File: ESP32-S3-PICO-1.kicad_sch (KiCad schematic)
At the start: 13 parts, among them CN3 Conn_Coaxial_Small, U5 ESP32-S3-PICO-1-N8R8, U6 BGS12WN6

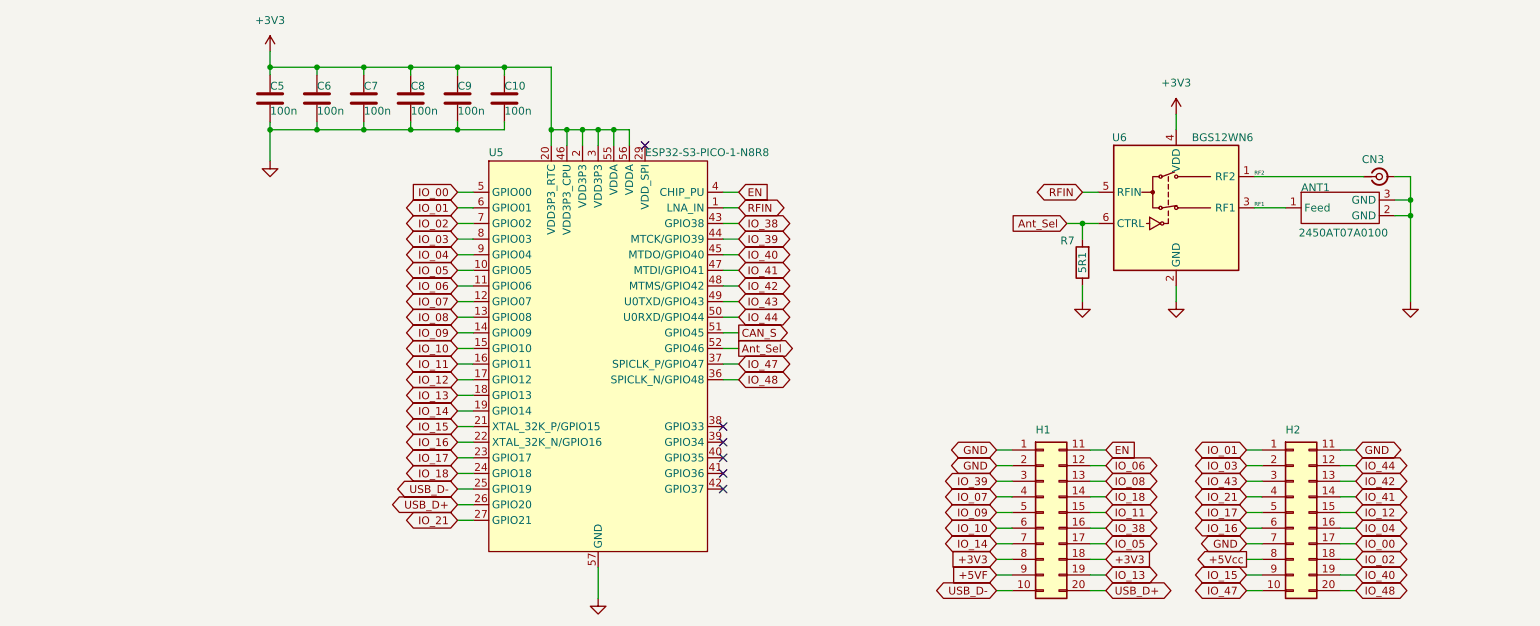
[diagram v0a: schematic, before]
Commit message: successful 1st pass, but I want to try some new bus'ing techniques to clean up the routing
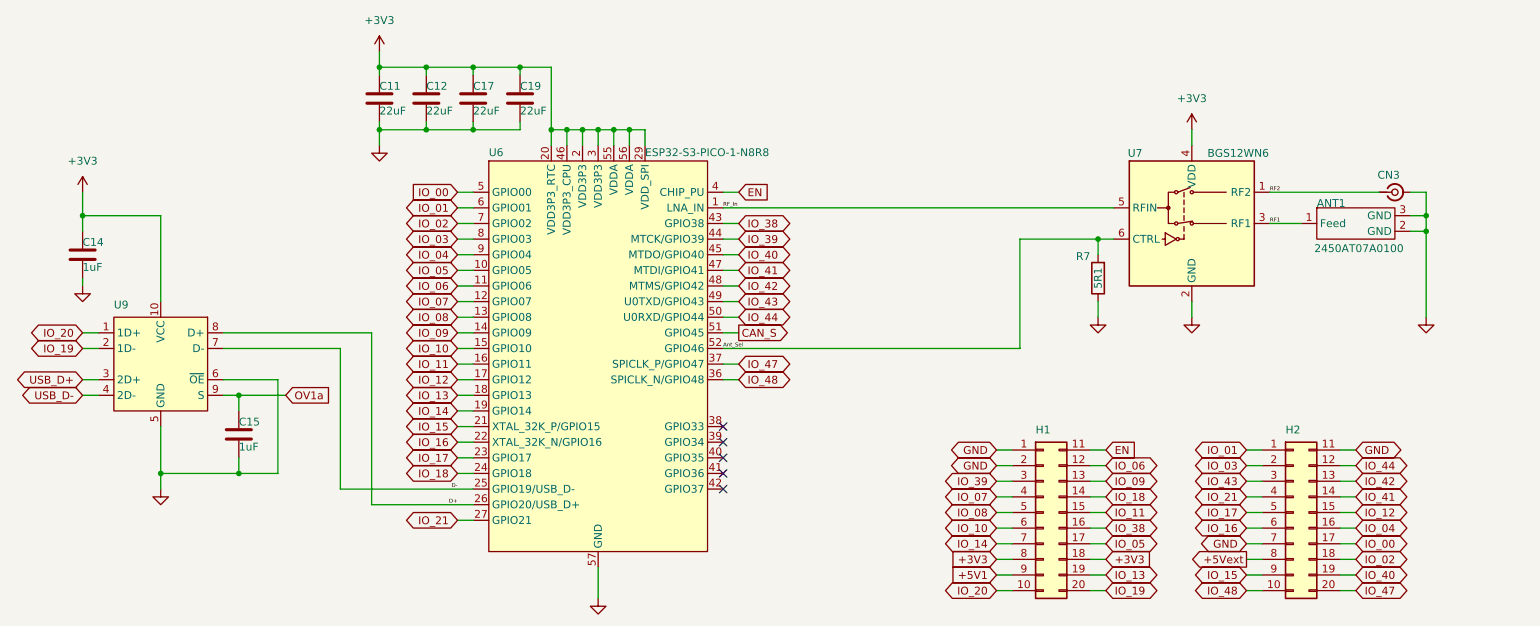
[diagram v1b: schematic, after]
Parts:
- removed C10, C5, C6, C7, C8, C9: 100n, Capacitors:C0201_Dense, symbol Device:C
- added C11, C12, C17, C19: 22uF, Capacitors:C0402_Dense, symbol Device:C
- added C14, C15: 1uF, Capacitors:C0201_Dense, symbol Device:C
- added U9: TS3USB221A-Q1, Personal_FootprintLibrary:Texas_UQFN-10_1.5x2mm_P0.5mm, symbol PersonalSchematicSymbolLibrary:TS3USB221A-Q1
- H1, H2: value ~ -> ESP_Header
- R7: footprint Resistors:R0201_Nominal -> Resistors:R0201_Dense
- renumbered U5 to U6, U6 to U7
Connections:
- net +3V3: now also U6.29 (VDD_SPI), C11.1, C12.1, C14.1, C17.1, C19.1, U9.10 (VCC)
- net GND: now also C11.2, C12.2, C14.2, C15.2, C17.2, C19.2, U9.5 (GND), U9.6 (~{OE})
- net IO_08: now also H1.5 (Pin_5); no longer H1.13 (Pin_13)
- net IO_09: now also H1.13 (Pin_13); no longer H1.5 (Pin_5)
- net IO_47: now also H2.20 (Pin_20); no longer H2.10 (Pin_10)
- net IO_48: now also H2.10 (Pin_10); no longer H2.20 (Pin_20)
- net USB_D+: now also U9.3 (2D+); no longer H1.20 (Pin_20), U6.26 (GPIO20)
- net USB_D-: now also U9.4 (2D-); no longer H1.10 (Pin_10), U6.25 (GPIO19)
- net +5VF renamed +5V1
- net +5Vcc renamed +5Vext
- net RFIN renamed RF_In
- new net D+: U6.26 (GPIO20/USB_D+), U9.8 (D+)
- new net D-: U6.25 (GPIO19/USB_D-), U9.7 (D-)
- new net IO_19: H1.20 (Pin_20), U9.2 (1D-)
- new net IO_20: H1.10 (Pin_10), U9.1 (1D+)
- new net OV1a: C15.1, U9.9 (S)
- no-connect marks 6 -> 5
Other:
- moved on the sheet: ANT1, CN3, R7, U7

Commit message: Update CAN_Interface.kicad_sch, ESP32-S3 Pico D1.kicad_dru, ESP32-S3 Pico D1.kicad_pcb, and 5 more files reroute completed
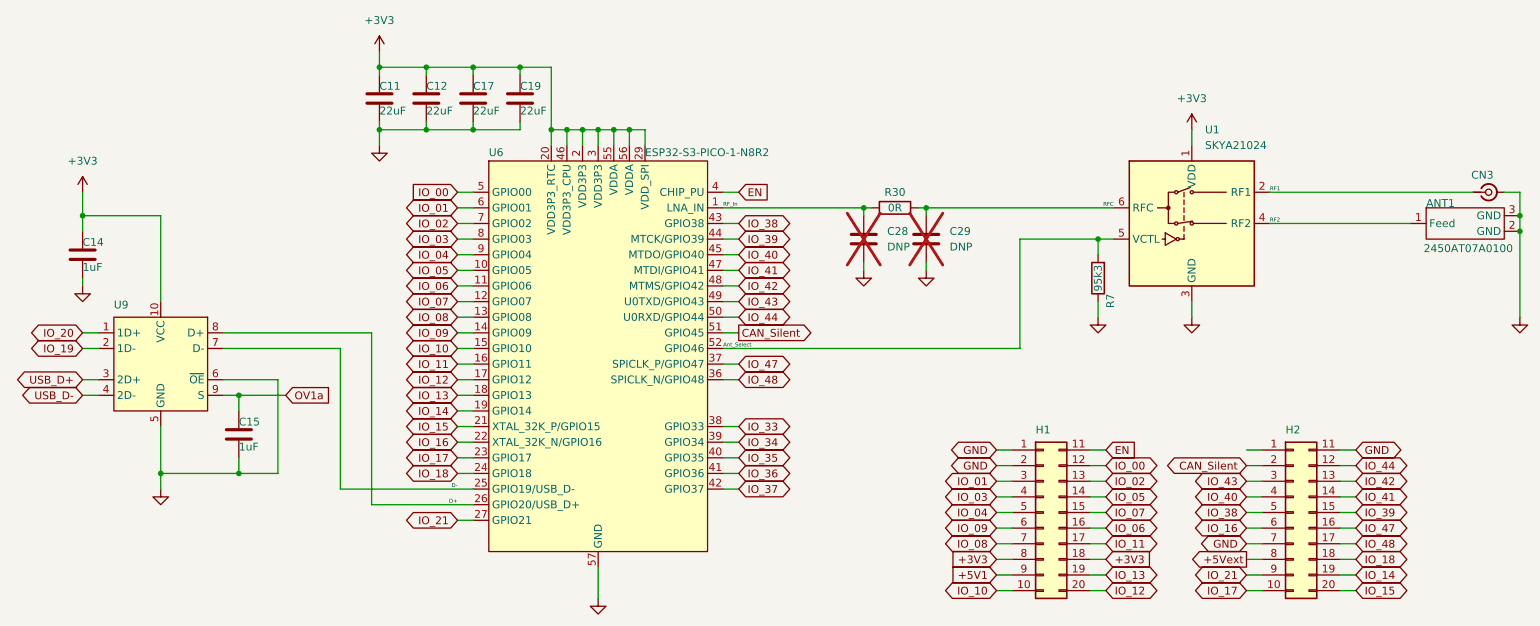
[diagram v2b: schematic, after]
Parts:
- removed U7: BGS12WN6, Personal_FootprintLibrary:TSNP-6, symbol RF_Switch:BGS12WN6E6327
- added C28, C29: DNP, Capacitors:C0201_Dense, symbol Device:C
- added R30: 0R, Resistors:R0201_Dense, symbol Device:R
- added U1: SKYA21024, Personal_FootprintLibrary:SKYA21024, symbol PersonalSchematicSymbolLibrary:SKYA21024
- CN3: value Conn_Coaxial_Small -> 2337019-1; footprint Personal_FootprintLibrary:U.FL_Molex_MCRF_73412 -> Personal_FootprintLibrary:u.FL_Male_Pin_Coax_SMD; Distributor Link 1 https://www.digikey.com/en/products/detail/molex/0734123150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 -> https://www.digikey.com/en/products/detail/te-connectivity-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; Distributor Link 2 https://www.mouser.com/ProductDetail/Molex/73412-3150?qs=2F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 -> https://www.mouser.com/ProductDetail/TE-Connectivity/233701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; LCSC C434806 -> C434807; Manufacturer Molex -> TE Connectivity; Manufacturer Part Number 734123150 -> 2337019-1
- H1, H2: now left out of the parts list
- R7: value 5R1 -> 95k3; Distributor Link 2 https://www.mouser.com/ProductDetail/Royalohm/PF01WMF5100TE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 -> https://www.mouser.com/ProductDetail/Royalohm/0201WMF9532TE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; LCSC C50670526 -> C423395; Manufacturer Part Number PF01WMF510KTEE -> 0201WMF9532TEE
- U6: value ESP32-S3-PICO-1-N8R8 -> ESP32-S3-PICO-1-N8R2
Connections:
- net +3V3: now also U1.1 (VDD)
- net GND: now also C28.2, C29.2, U1.3 (GND)
- net IO_00: now also H1.12 (Pin_12); no longer H2.17 (Pin_17)
- net IO_01: now also H1.3 (Pin_3); no longer H2.1 (Pin_1)
- net IO_02: now also H1.13 (Pin_13); no longer H2.18 (Pin_18)
- net IO_03: now also H1.4 (Pin_4); no longer H2.2 (Pin_2)
- net IO_04: now also H1.5 (Pin_5); no longer H2.16 (Pin_16)
- net IO_05: now also H1.14 (Pin_14); no longer H1.17 (Pin_17)
- net IO_06: now also H1.16 (Pin_16); no longer H1.12 (Pin_12)
- net IO_07: now also H1.15 (Pin_15); no longer H1.4 (Pin_4)
- net IO_08: now also H1.7 (Pin_7); no longer H1.5 (Pin_5)
- net IO_09: now also H1.6 (Pin_6); no longer H1.13 (Pin_13)
- net IO_10: now also H1.10 (Pin_10); no longer H1.6 (Pin_6)
- net IO_11: now also H1.17 (Pin_17); no longer H1.15 (Pin_15)
- net IO_12: now also H1.20 (Pin_20); no longer H2.15 (Pin_15)
- net IO_14: now also H2.19 (Pin_19); no longer H1.7 (Pin_7)
- net IO_15: now also H2.20 (Pin_20); no longer H2.9 (Pin_9)
- net IO_17: now also H2.10 (Pin_10); no longer H2.5 (Pin_5)
- net IO_18: now also H2.18 (Pin_18); no longer H1.14 (Pin_14)
- net IO_19: no longer H1.20 (Pin_20)
- net IO_20: no longer H1.10 (Pin_10)
- net IO_21: now also H2.9 (Pin_9); no longer H2.4 (Pin_4)
- net IO_38: now also H2.5 (Pin_5); no longer H1.16 (Pin_16)
- net IO_39: now also H2.15 (Pin_15); no longer H1.3 (Pin_3)
- net IO_40: now also H2.4 (Pin_4); no longer H2.19 (Pin_19)
- net IO_47: now also H2.16 (Pin_16); no longer H2.20 (Pin_20)
- net IO_48: now also H2.17 (Pin_17); no longer H2.10 (Pin_10)
- net RF1: now also CN3.1 (In), U1.2 (RF1); no longer ANT1.1 (Feed), ANT1.4 (Feed)
- net RF2: now also ANT1.1 (Feed), ANT1.4 (Feed), U1.4 (RF2); no longer CN3.1 (In)
- net RF_In: now also C28.1, R30.1
- net IO_33: now reaches U6.38 (GPIO33)
- net IO_34: now reaches U6.39 (GPIO34)
- net IO_35: now reaches U6.40 (GPIO35)
- net IO_36: now reaches U6.41 (GPIO36)
- net IO_37: now reaches U6.42 (GPIO37)
- net Ant_Sel renamed Ant_Select
- net Ant_Select: now also U1.5 (VCTL)
- net CAN_S renamed CAN_Silent
- net CAN_Silent: now also H2.2 (Pin_2)
- new net RFC: C29.1, R30.2, U1.6 (RFC)
- no-connect marks 5 -> 0
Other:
- moved on the sheet: ANT1, CN3
